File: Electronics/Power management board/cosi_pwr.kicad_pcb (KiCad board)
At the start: 2 copper layers, 118.4 x 104.3 mm, 54 parts, among them K1 PT371512, K2 G5SB, U1 IRM_15_20, U10 N-CHANNEL-MOSFET-BSS138, U11 N-CHANNEL-MOSFET-BSS138, U2 DCDC_SIM1_DIP8, U3 N-CHANNEL-MOSFET-BSS138, U5 N-CHANNEL-MOSFET-BSS138, U6 N-CHANNEL-MOSFET-BSS138, U7 N-CHANNEL-MOSFET-BSS138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

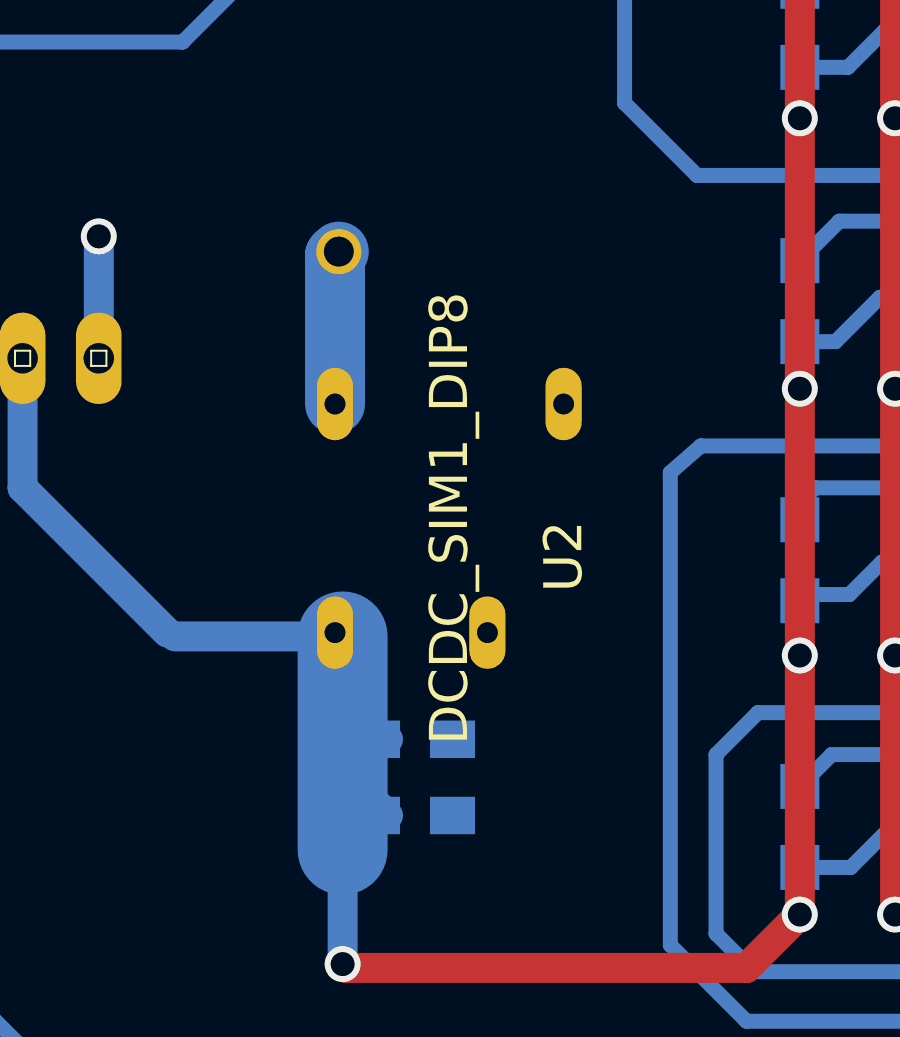
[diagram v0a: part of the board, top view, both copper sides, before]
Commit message: Updated KiCAD + Gerber files of the power managment board.
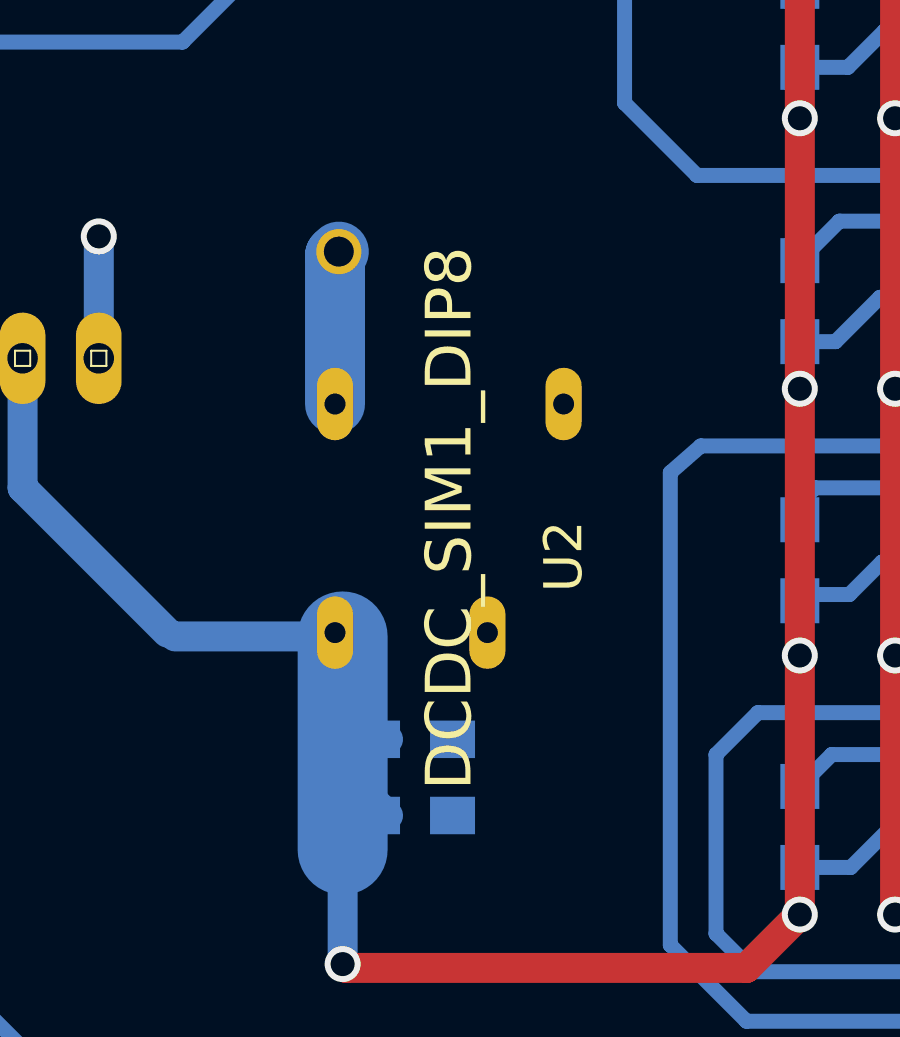
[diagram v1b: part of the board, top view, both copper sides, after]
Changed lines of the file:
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@@
-(kicad_pcb (version 4) (host pcbnew 4.0.2+e4-6225~38~ubuntu16.04.1-stable)
+(kicad_pcb (version 20171130) (host pcbnew "(5.0.0)")
   (general
-    (links 106)
-    (no_connects 0)
-    (area 62.750429 28.674619 195.948572 143.504)
     (thickness 1.6)
     (drawings 10)
@@
     (0 Top signal)
     (31 Bottom signal)
-    (32 B.Adhes user)
-    (33 F.Adhes user)
-    (34 B.Paste user)
-    (35 F.Paste user)
+    (32 B.Adhes user hide)
+    (33 F.Adhes user hide)
+    (34 B.Paste user hide)
+    (35 F.Paste user hide)
     (36 B.SilkS user)
     (37 F.SilkS user)
-    (38 B.Mask user)
-    (39 F.Mask user)
-    (40 Dwgs.User user)
-    (41 Cmts.User user)
-    (42 Eco1.User user)
-    (43 Eco2.User user)
+    (38 B.Mask user hide)
+    (39 F.Mask user hide)
+    (40 Dwgs.User user hide)
+    (41 Cmts.User user hide)
+    (42 Eco1.User user hide)
+    (43 Eco2.User user hide)
     (44 Edge.Cuts user)
-    (45 Margin user)
+    (45 Margin user hide)
     (46 B.CrtYd user)
     (47 F.CrtYd user)
-    (48 B.Fab user)
-    (49 F.Fab user)
+    (48 B.Fab user hide)
+    (49 F.Fab user hide)
   )
   (setup
@@
     (visible_elements 7FFEFFFF)
     (pcbplotparams
-      (layerselection 0x01000_80000001)
+      (layerselection 0x0d030_ffffffff)
       (usegerberextensions false)
+      (usegerberattributes false)
+      (usegerberadvancedattributes false)
+      (creategerberjobfile false)
       (excludeedgelayer true)
       (linewidth 0.100000)
@@
       (hpglpennumber 1)
       (hpglpenspeed 20)
-      (hpglpendiameter 15)
-      (hpglpenoverlay 2)
+      (hpglpendiameter 15.000000)
       (psnegative false)
       (psa4output false)
@@
       (drillshape 0)
       (scaleselection 1)
-      (outputdirectory Gerber/))
+      (outputdirectory "Gerber/2019-01-25/"))
   )
   (net 0 "")
@@
     )
     (fp_text value DCDC_SIM1_DIP8 (at 0 0 270) (layer F.SilkS)
-      (effects (font (thickness 0.15)))
+      (effects (font (size 1.524 1.524) (thickness 0.15)))
     )
     (fp_line (start -5.08 -5.08) (end -5.08 5.08) (layer B.SilkS) (width 0.254))
@@
     (tags DIODE)
     (attr virtual)
-    (fp_text reference D2 (at 1.143 -2.286 360) (layer F.SilkS)
+    (fp_text reference D2 (at 1.143 -2.286) (layer F.SilkS)
       (effects (font (size 1.27 1.27) (thickness 0.127)))
     )
@@
         (xy 120.65 107.188) (xy 101.854 107.188) (xy 101.854 93.472) (xy 107.188 93.472) (xy 107.188 99.187)
         (xy 113.792 99.187) (xy 114.4905 55.499) (xy 70.739 55.499) (xy 70.739 49.149) (xy 82.931 49.149)
-        (xy 82.931 40.132) (xy 120.65 40.132) (xy 120.65 107.188)
+        (xy 82.931 40.132) (xy 120.65 40.132)
       )
     )
@@
       (pts
         (xy 107.696 85.344) (xy 102.108 85.344) (xy 102.108 69.85) (xy 70.612 69.85) (xy 70.612 60.96)
-        (xy 107.696 60.96) (xy 107.696 85.344)
+        (xy 107.696 60.96)
       )
     )
@@
         (xy 99.568 85.979) (xy 89.535 85.979) (xy 89.535 95.504) (xy 78.486 95.504) (xy 78.486 90.17)
         (xy 85.09 90.17) (xy 85.09 77.597) (xy 76.708 77.597) (xy 76.708 73.025) (xy 99.568 73.025)
-        (xy 99.568 85.979)
       )
     )
@@
         (xy 82.804 87.757) (xy 75.692 87.757) (xy 75.692 100.838) (xy 93.218 100.838) (xy 93.218 92.456)
         (xy 98.806 92.456) (xy 98.806 107.188) (xy 70.612 107.188) (xy 70.612 82.423) (xy 82.804 82.423)
-        (xy 82.804 87.757)
       )
     )
@@
     (polygon
       (pts
-        (xy 187.579 141.986) (xy 177.165 141.986) (xy 177.165 132.715) (xy 187.579 132.715) (xy 187.579 141.986)
+        (xy 187.579 141.986) (xy 177.165 141.986) (xy 177.165 132.715) (xy 187.579 132.715)
       )
     )
@@
     (polygon
       (pts
-        (xy 162.179 133.223) (xy 160.147 133.223) (xy 160.147 132.334) (xy 162.179 132.334) (xy 162.179 133.223)
+        (xy 162.179 133.223) (xy 160.147 133.223) (xy 160.147 132.334) (xy 162.179 132.334)
       )
     )
@@
       (pts
         (xy 154.432 133.35) (xy 155.194 133.35) (xy 155.194 136.144) (xy 154.305 136.144) (xy 154.305 133.35)
-        (xy 154.432 133.35)
       )
     )
@@
     (polygon
       (pts
-        (xy 185.166 126.746) (xy 182.88 126.746) (xy 182.88 125.984) (xy 185.166 125.984) (xy 185.166 126.746)
+        (xy 185.166 126.746) (xy 182.88 126.746) (xy 182.88 125.984) (xy 185.166 125.984)
       )
     )
@@
     (polygon
       (pts
-        (xy 158.115 114.935) (xy 156.718 114.935) (xy 156.718 107.442) (xy 158.115 107.442) (xy 158.115 114.935)
+        (xy 158.115 114.935) (xy 156.718 114.935) (xy 156.718 107.442) (xy 158.115 107.442)
       )
     )
@@
     (polygon
       (pts
-        (xy 157.861 131.572) (xy 155.194 131.572) (xy 155.194 84.963) (xy 157.861 84.963) (xy 157.861 131.572)
+        (xy 157.861 131.572) (xy 155.194 131.572) (xy 155.194 84.963) (xy 157.861 84.963)
       )
     )
@@
     (polygon
       (pts
-        (xy 166.243 132.334) (xy 163.576 132.334) (xy 163.576 84.963) (xy 166.243 84.963) (xy 166.243 132.334)
+        (xy 166.243 132.334) (xy 163.576 132.334) (xy 163.576 84.963) (xy 166.243 84.963)
       )
     )
@@
     (polygon
       (pts
-        (xy 70.6755 60.325) (xy 70.6755 60.2615) (xy 70.739 60.325) (xy 70.6755 60.325)
+        (xy 70.6755 60.325) (xy 70.6755 60.2615) (xy 70.739 60.325)
       )
     )
@@
       (pts
         (xy 70.739 39.624) (xy 70.739 107.188) (xy 120.65 107.188) (xy 120.65 39.497) (xy 70.739 39.497)
-        (xy 70.739 39.624)
       )
     )
